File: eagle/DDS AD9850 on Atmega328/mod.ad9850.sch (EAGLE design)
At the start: 1 part

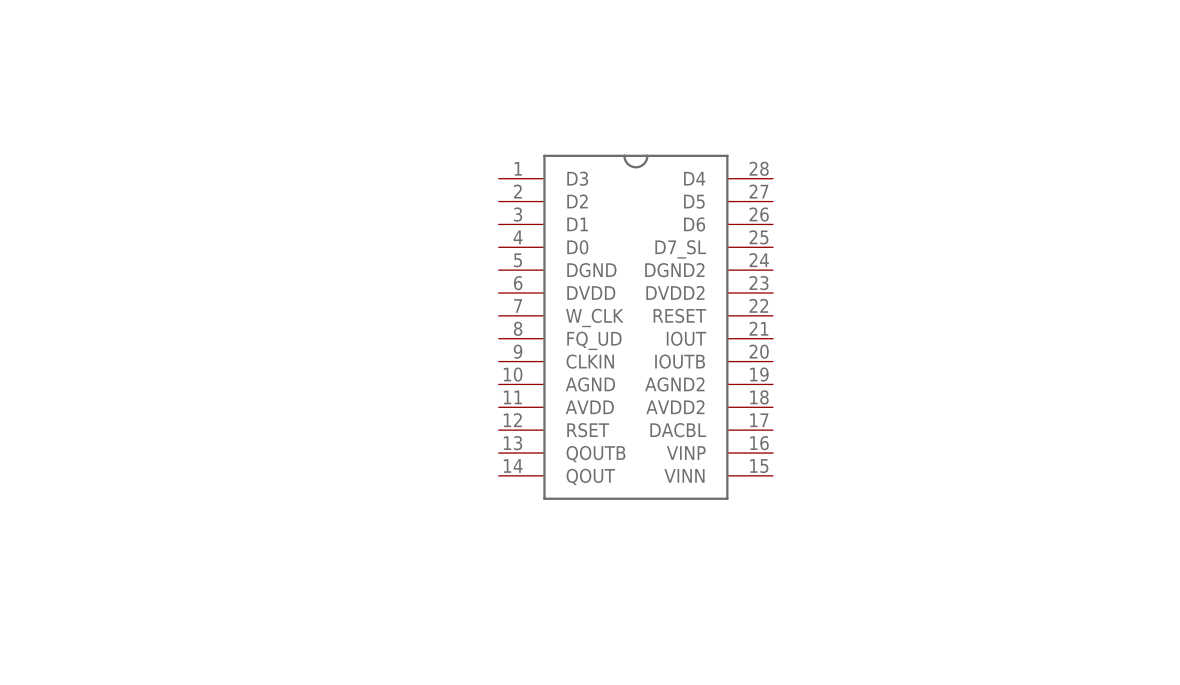
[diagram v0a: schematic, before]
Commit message: 
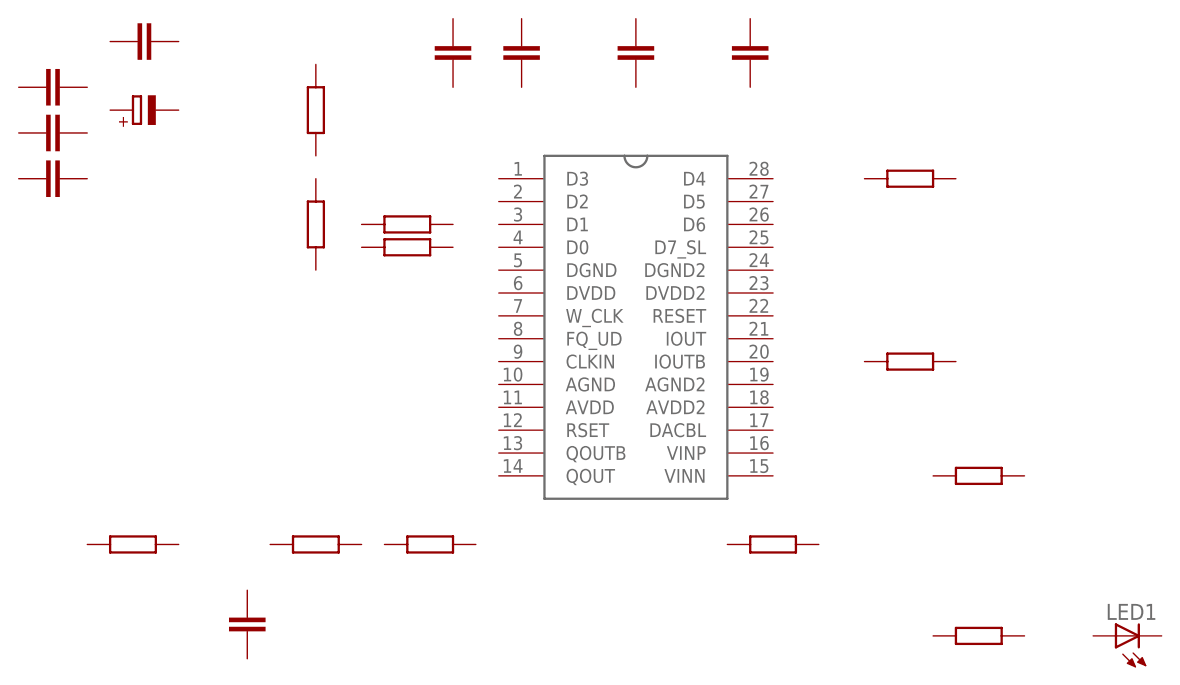
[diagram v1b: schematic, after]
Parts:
- added LED1: (no value), eagle-ltspice:LED_ESML0603
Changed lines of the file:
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@@
 <layer number="97" name="Info" color="7" fill="1" visible="yes" active="yes"/>
 <layer number="98" name="Guide" color="6" fill="1" visible="yes" active="yes"/>
+<layer number="99" name="SpiceOrder" color="5" fill="1" visible="yes" active="yes"/>
 </layers>
 <schematic xreflabel="%F%N/%S.%C%R" xrefpart="/%S.%C%R">
@@
 <parts>
 <part name="U$1" library="ad9850" deviceset="AD9850" device=""/>
+<part name="R1" library="docu-dummy" deviceset="R" device=""/>
+<part name="R2" library="docu-dummy" deviceset="R" device=""/>
+<part name="R3" library="docu-dummy" deviceset="R" device=""/>
+<part name="R4" library="docu-dummy" deviceset="R" device=""/>
+<part name="R5" library="docu-dummy" deviceset="R" device=""/>
+<part name="R6" library="docu-dummy" deviceset="R" device=""/>
+<part name="R7" library="docu-dummy" deviceset="R" device=""/>
+<part name="R8" library="docu-dummy" deviceset="R" device=""/>
+<part name="R9" library="docu-dummy" deviceset="R" device=""/>
+<part name="R10" library="docu-dummy" deviceset="R" device=""/>
+<part name="R11" library="docu-dummy" deviceset="R" device=""/>
+<part name="R12" library="docu-dummy" deviceset="R" device=""/>
+<part name="C1" library="docu-dummy" deviceset="C" device=""/>
+<part name="C2" library="docu-dummy" deviceset="C" device=""/>
+<part name="C3" library="docu-dummy" deviceset="C" device=""/>
+<part name="C4" library="docu-dummy" deviceset="C" device=""/>
+<part name="C5" library="docu-dummy" deviceset="C" device=""/>
+<part name="C6" library="docu-dummy" deviceset="C" device=""/>
+<part name="C7" library="docu-dummy" deviceset="C" device=""/>
+<part name="C8" library="docu-dummy" deviceset="C" device=""/>
+<part name="C9" library="docu-dummy" deviceset="C" device=""/>
+<part name="C10" library="docu-dummy" deviceset="ELKO" device=""/>
+<part name="LED1" library="eagle-ltspice" deviceset="LED_E" device="SML0603"/>
 </parts>
 <sheets>
@@
 <instances>
 <instance part="U$1" gate="G$1" x="0" y="0"/>
+<instance part="R1" gate="G$1" x="-25.4" y="12.7"/>
+<instance part="R2" gate="G$1" x="-25.4" y="10.16"/>
+<instance part="R3" gate="G$1" x="-35.56" y="12.7" rot="R90"/>
+<instance part="R4" gate="G$1" x="-35.56" y="-22.86"/>
+<instance part="R5" gate="G$1" x="-22.86" y="-22.86"/>
+<instance part="R6" gate="G$1" x="-55.88" y="-22.86"/>
+<instance part="R7" gate="G$1" x="15.24" y="-22.86"/>
+<instance part="R8" gate="G$1" x="38.1" y="-15.24"/>
+<instance part="R9" gate="G$1" x="38.1" y="-33.02"/>
+<instance part="R10" gate="G$1" x="30.48" y="-2.54"/>
+<instance part="R11" gate="G$1" x="30.48" y="17.78"/>
+<instance part="R12" gate="G$1" x="-35.56" y="25.4" rot="R90"/>
+<instance part="C1" gate="G$1" x="-20.32" y="33.02"/>
+<instance part="C2" gate="G$1" x="-12.7" y="33.02"/>
+<instance part="C3" gate="G$1" x="0" y="33.02"/>
+<instance part="C4" gate="G$1" x="12.7" y="33.02"/>
+<instance part="C5" gate="G$1" x="-55.88" y="33.02" rot="R90"/>
+<instance part="C6" gate="G$1" x="-63.5" y="27.94" rot="R270"/>
+<instance part="C7" gate="G$1" x="-63.5" y="22.86" rot="R270"/>
+<instance part="C8" gate="G$1" x="-63.5" y="17.78" rot="R270"/>
+<instance part="C9" gate="G$1" x="-43.18" y="-30.48"/>
+<instance part="C10" gate="G$1" x="-55.88" y="25.4" rot="R90"/>
+<instance part="LED1" gate="G$1" x="53.34" y="-33.02" rot="R90"/>
 </instances>
 <busses>
